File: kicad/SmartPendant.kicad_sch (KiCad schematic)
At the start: 83 parts, among them P1 FPC 0.5MM 40P Pull type H2.0m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, P2 KH-FG0.5-H2.0-6PIN, Q1 SS8050_C2150, U1 74AHC2G125DP,125, U2 AMS1117-3.3, U3 MB85RC256VPNF

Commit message: Fix cosmetics.
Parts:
- removed A1: A, symbol Unknown_0_-806
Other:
- note added: "Original diagram by nick_shl/Devtronic LLC (2024-11-07) KiCad version by Torsten Martinsen, 2025"
- note added: "Smart Pendant"
- moved on the sheet: +3.3V1, +5V1, A0, B+3.3V1, B+5V1, BATTERY1, BLE1, BLE_BTN1, BRST1, BTN1, BTN_L1, BTN_LD1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

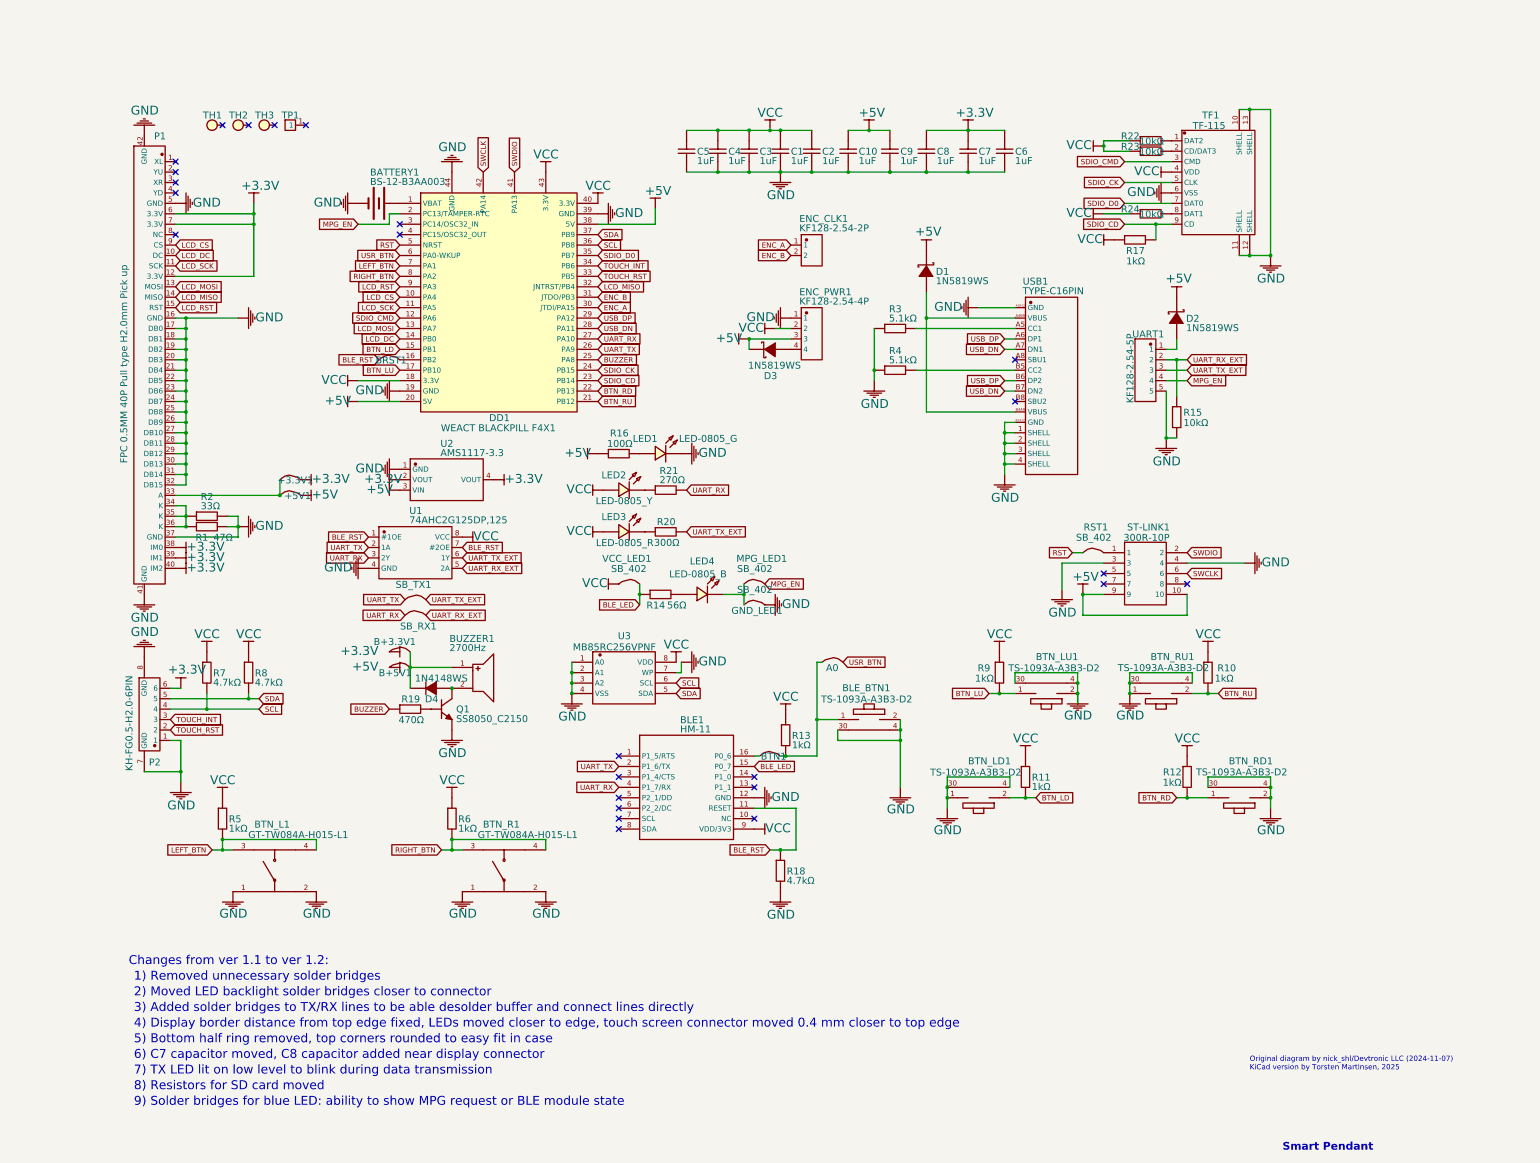
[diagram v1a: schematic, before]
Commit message: Update schematic to match V1.3.
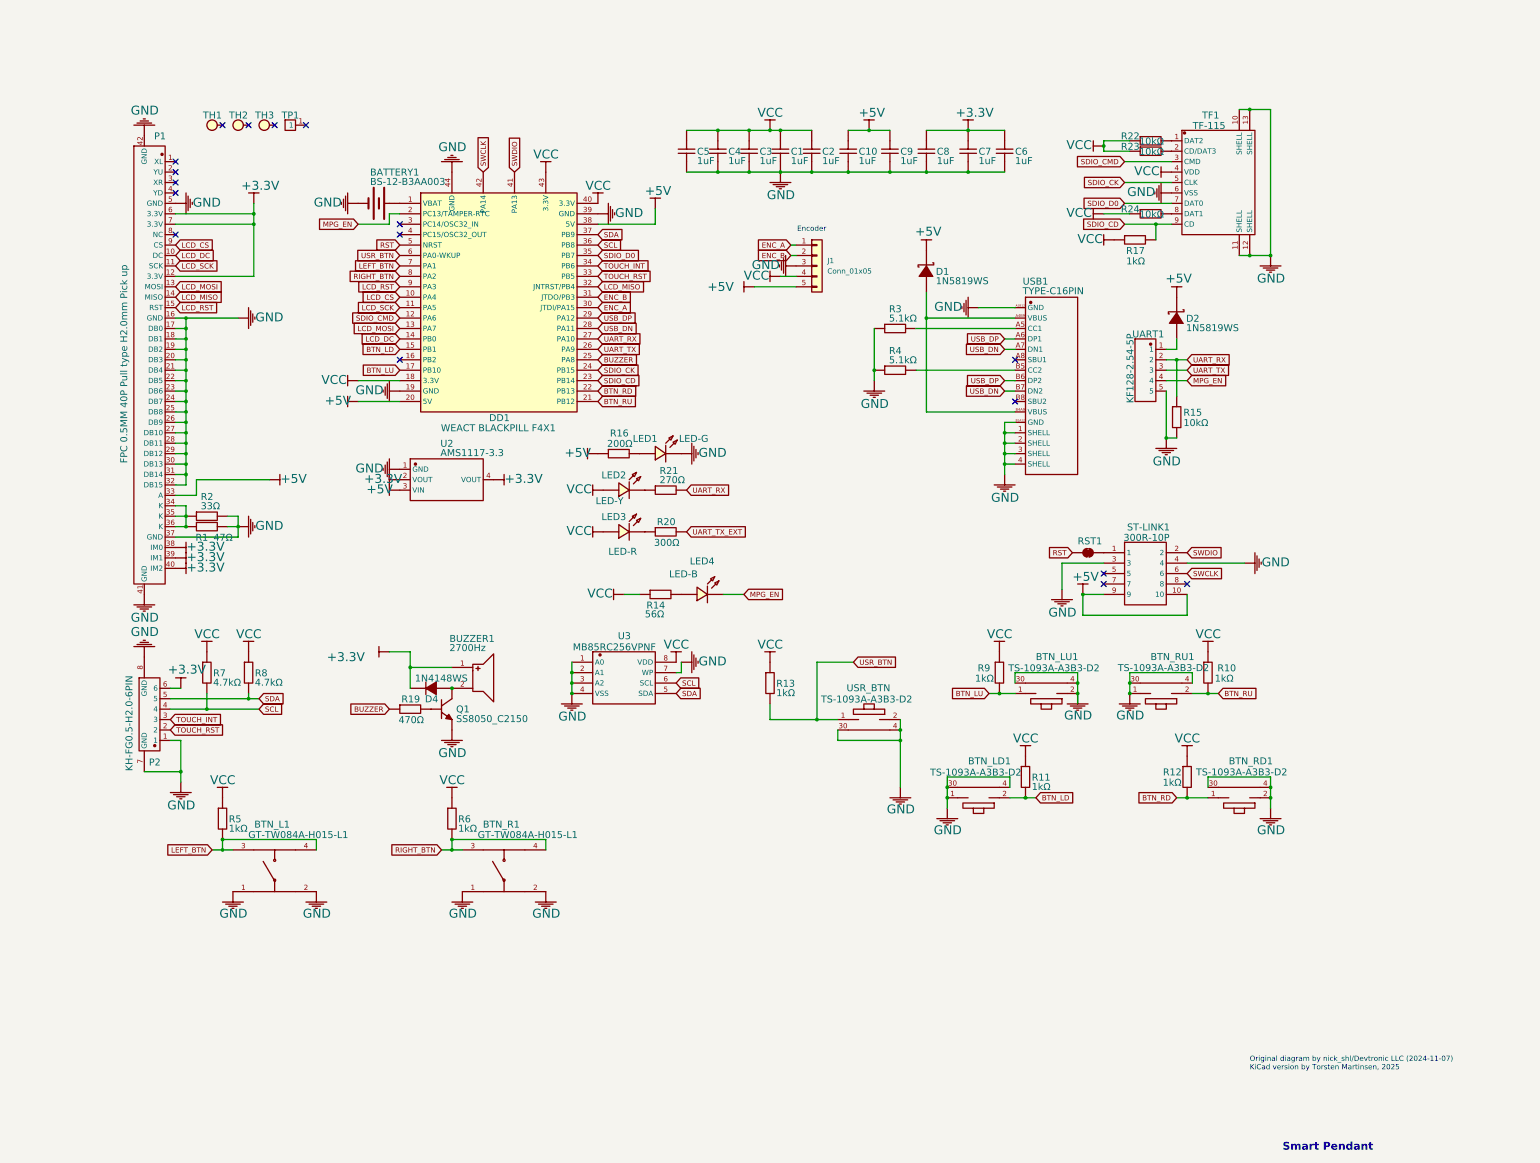
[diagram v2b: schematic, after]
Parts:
- removed +3.3V1: SB_402, symbol Solder_Joint_0402_2
- removed +5V1: SB_402, symbol Solder_Joint_0402_1
- removed A0: SB_402, symbol Solder_Joint_0402_4
- removed B+3.3V1: SB_402, symbol Solder_Joint_0402_5
- removed B+5V1: SB_402, symbol Solder_Joint_0402_6
- removed BLE1: HM-11, symbol HM-11
- removed BRST1: SB_402, symbol Solder_Joint_0402_7
- removed BTN1: SB_402, symbol Solder_Joint_0402_3
- removed D3: 1N5819WS, symbol B5819WS_C22624_2
- removed ENC_CLK1: KF128-2.54-2P, symbol KF128-2.54-2P
- removed ENC_PWR1: KF128-2.54-4P, symbol KF128-2.54-4P
- removed GND_LED1: SB_402, symbol Solder_Joint_0402_11
- removed MPG_LED1: SB_402, symbol Solder_Joint_0402_10
- removed R18: 4.7kΩ, symbol 0805W8F1002T5E_12
- removed SB_RX1: SB_402, symbol Solder_Joint_0402_9
- removed SB_TX1: SB_402, symbol Solder_Joint_0402_8
- removed U1: 74AHC2G125DP,125, symbol 74AHC2G125DP,125
- removed VCC_LED1: SB_402, symbol Solder_Joint_0402_12
- added J1: Conn_01x05, symbol Connector_Generic:Conn_01x05
- LED1: value LED-0805_G -> LED-G
- LED2: value LED-0805_Y -> LED-Y
- LED3: value LED-0805_R -> LED-R
- LED4: value LED-0805_B -> LED-B
- R16: value 100Ω -> 200Ω
- RST1: symbol Solder_Joint_0402 -> Jumper:SolderJumper_2_Bridged; now left out of the parts list
- renumbered BLE_BTN1 to USR_BTN
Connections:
- net BLE_LED is gone; now on net VCC: R14.1
- net UART_RX_EXT is gone; now on net UART_RX: R15.1, UART1.2
- net +3.3V: now also BUZZER1.1, D4.1 (K)
- net +5V: now also P1.33 (A), J1.5 (Pin_5)
- net ENC_A: now also J1.1 (Pin_1)
- net ENC_B: now also J1.2 (Pin_2)
- net GND: now also J1.3 (Pin_3)
- net MPG_EN: now also LED4.2
- net UART_TX: now also UART1.3
- net UART_TX_EXT: no longer UART1.3
- net USR_BTN: now also R13.2, USR_BTN.1
- net VCC: now also J1.4 (Pin_4)
- no-connect marks 25 -> 17
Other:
- note added: "Encoder"
- note removed: "1) Removed unnecessary solder bridges"
- note removed: "2) Moved LED backlight solder bridges closer to connector"
- note removed: "3) Added solder bridges to TX/RX lines to be able desolder buffer and connect lines directly"
- note removed: "4) Display border distance from top edge fixed, LEDs moved closer to edge, touch screen connector moved 0.4 mm closer to top edge"
- note removed: "5) Bottom half ring removed, top corners rounded to easy fit in case"
- note removed: "6) C7 capacitor moved, C8 capacitor added near display connector"
- note removed: "7) TX LED lit on low level to blink during data transmission"
- note removed: "8) Resistors for SD card moved"
- note removed: "9) Solder bridges for blue LED: ability to show MPG request or BLE module state"
- note removed: "Changes from ver 1.1 to ver 1.2:"
- moved on the sheet: R13

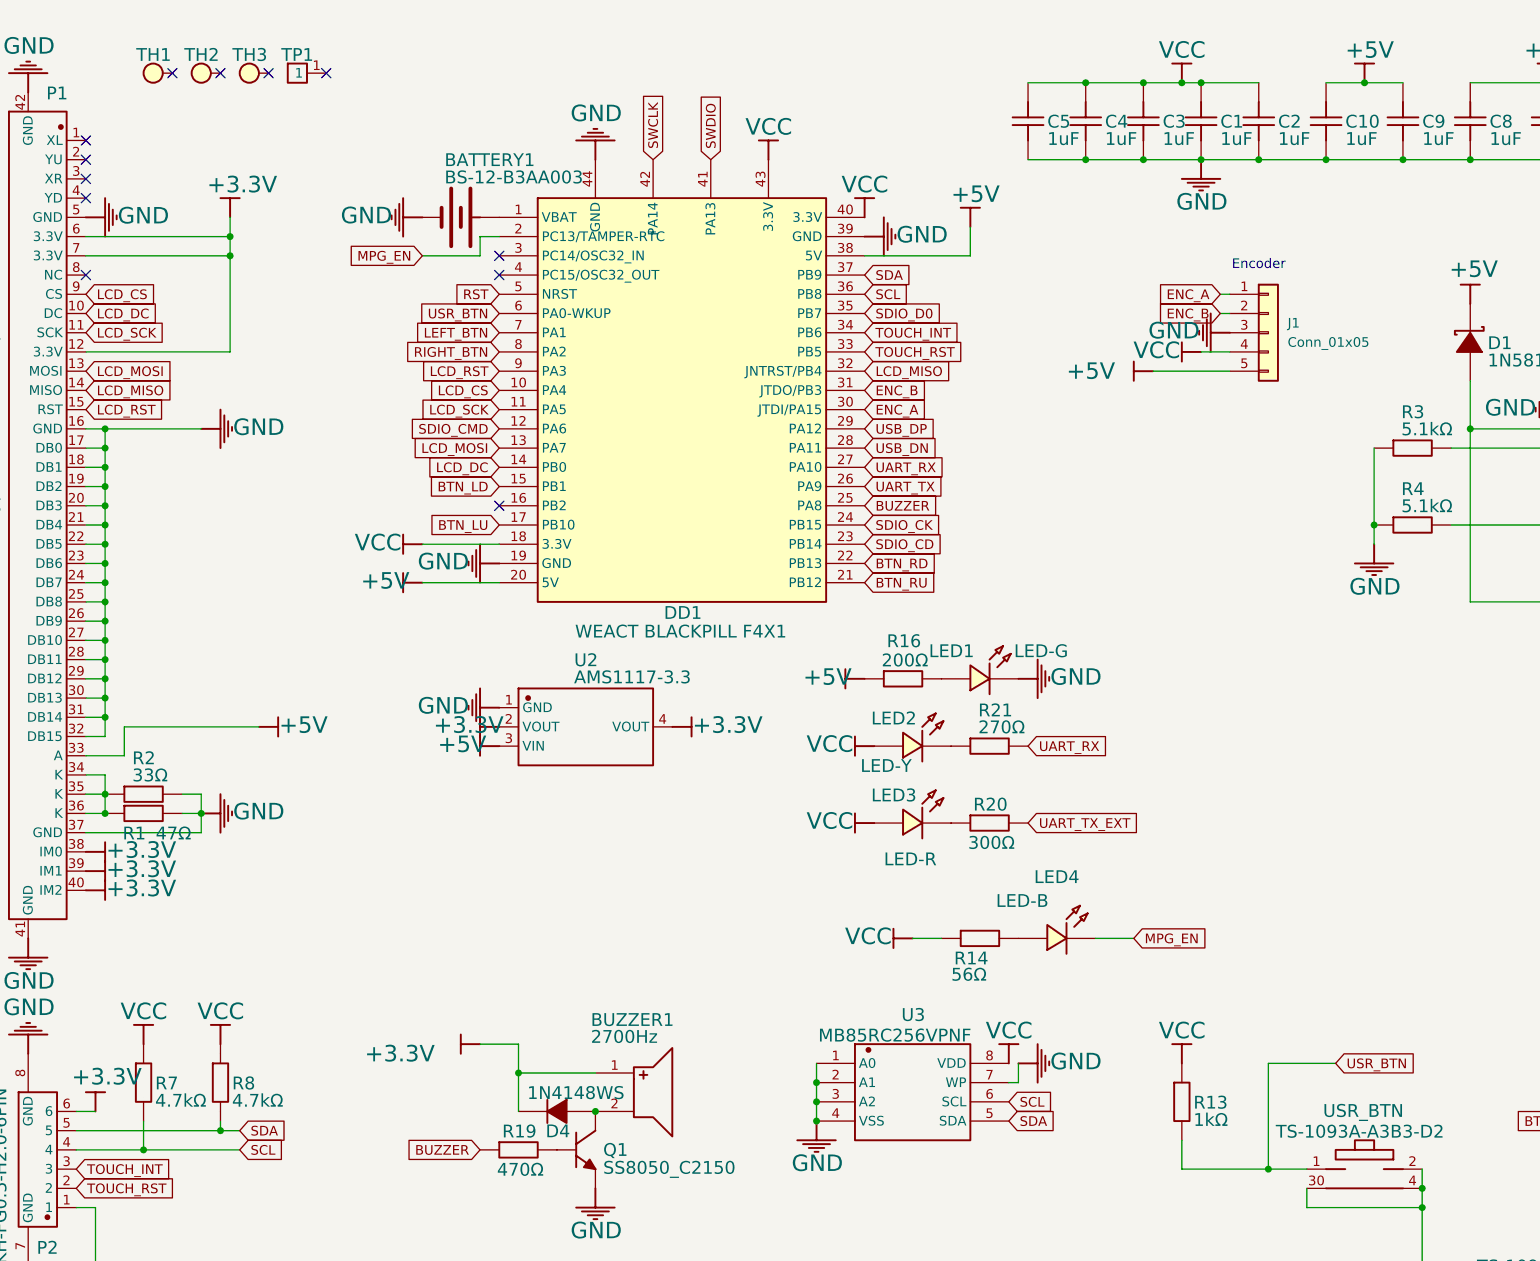
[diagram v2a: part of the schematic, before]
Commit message: Add footprints.
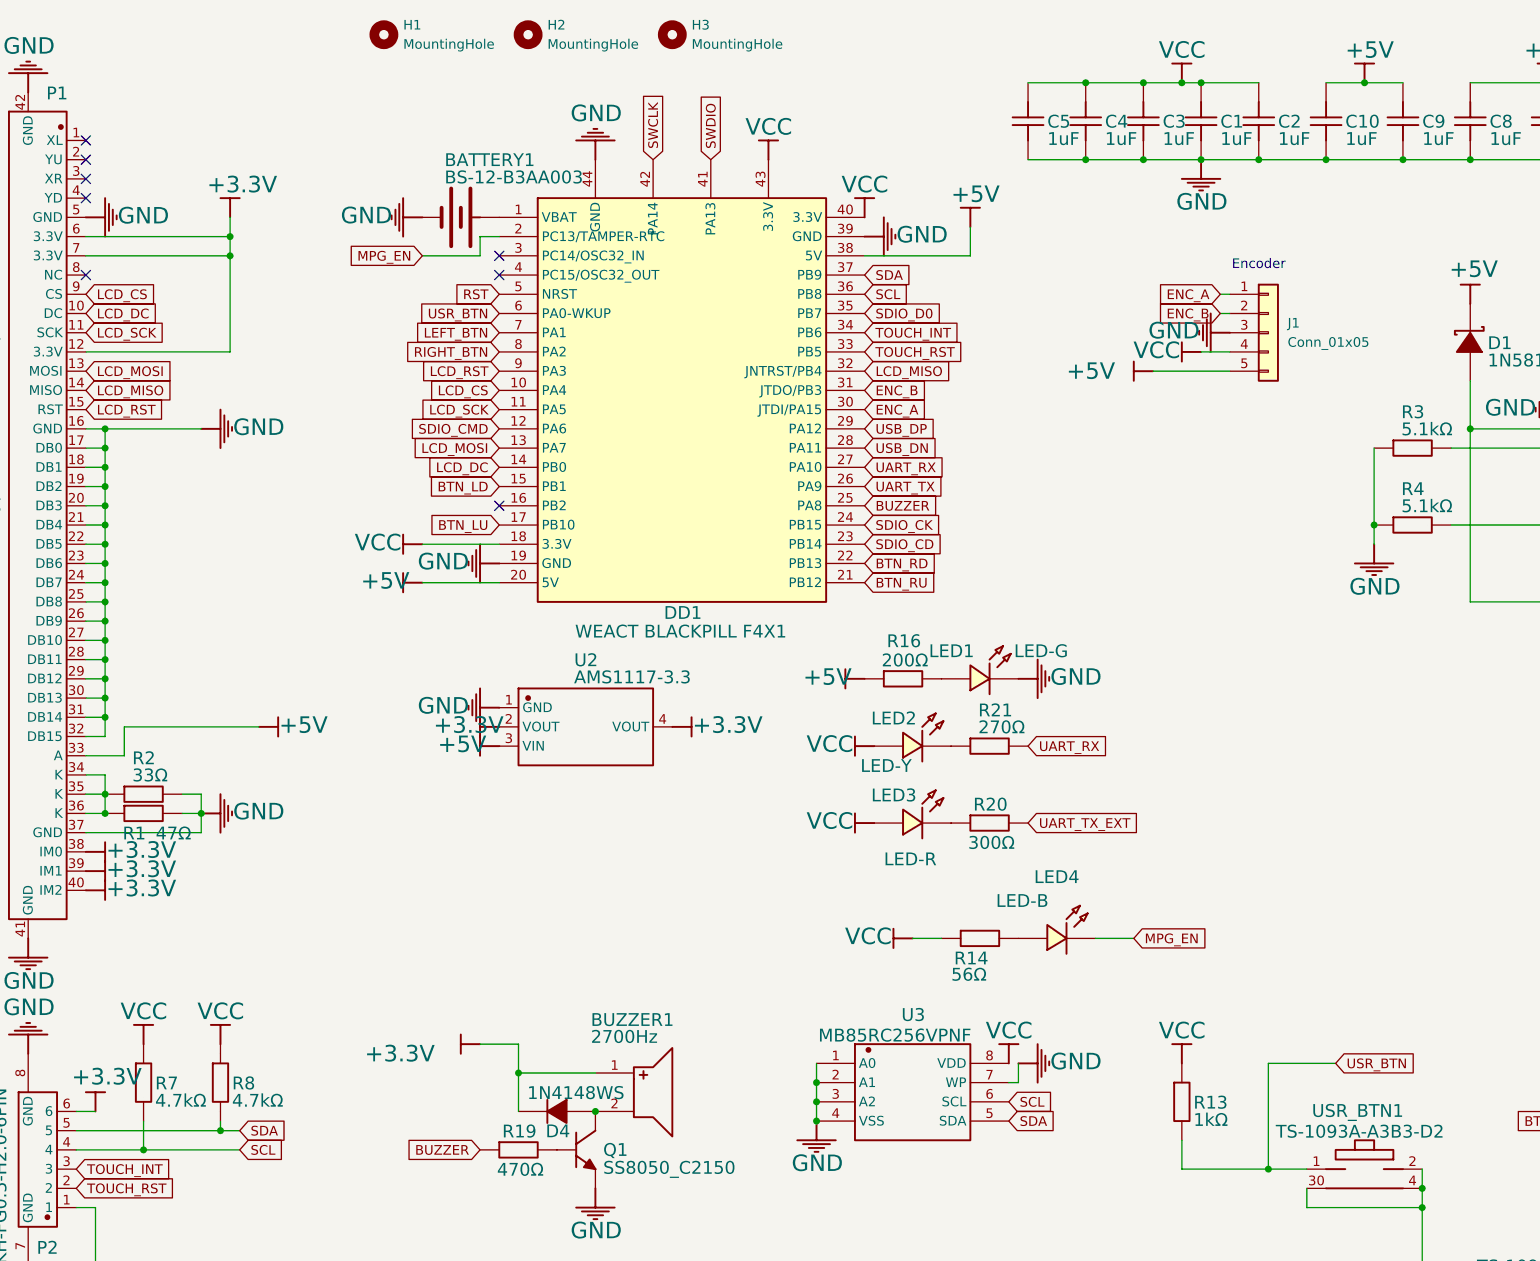
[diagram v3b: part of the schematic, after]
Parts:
- removed TH1: JLC SMT copper tooling hole, symbol JLC SMT copper tooling hole
- removed TH2: JLC SMT copper tooling hole, symbol JLC SMT copper tooling hole_1
- removed TH3: JLC SMT copper tooling hole, symbol JLC SMT copper tooling hole_2
- removed TP1: TESTPOINT, symbol TESTPOINT
- added H1, H2, H3: MountingHole, MountingHole:MountingHole_3.2mm_M3, symbol Mechanical:MountingHole
- C1, C10, C2, C3, C4, C5, C6, C7, C8, C9: footprint (none) -> PCM_Capacitor_SMD_AKL:C_0603_1608Metric
- D1, D2, D4: footprint (none) -> PCM_Diode_SMD_AKL:D_MiniMELF
- J1: footprint (none) -> Connector_JST:JST_XH_B5B-XH-A_1x05_P2.50mm_Vertical
- LED1, LED2, LED3, LED4: footprint (none) -> PCM_Diode_SMD_AKL:D_0603_1608Metric
- R1, R10, R11, R12, R13, R14, R15, R16, R17, R19, R2, R20, R21, R22, R23, R24, R3, R4, R5, R6, R7, R8, R9: footprint (none) -> PCM_Resistor_SMD_AKL:R_0603_1608Metric
- RST1: footprint (none) -> Jumper:SolderJumper-2_P1.3mm_Bridged_RoundedPad1.0x1.5mm
- U2: footprint (none) -> PCM_Package_TO_SOT_SMD_AKL:SOT-223
- renumbered USR_BTN to USR_BTN1
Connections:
- no-connect marks 17 -> 13
